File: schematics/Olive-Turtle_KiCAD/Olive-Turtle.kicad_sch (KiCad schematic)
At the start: 14 parts, among them IC1 ENS160-BGLT, U1 ESP32-DEVKITC-32U

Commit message: Designed VeeCAD schematic
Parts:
- renumbered L1-T2 to L1-T1, L1-T1 to L2-T1
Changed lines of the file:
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@@
   (symbol (lib_id "IRF520:IRF520") (at 74.93 78.74 0) (mirror y) (unit 1)
     (in_bom yes) (on_board yes) (dnp no)
-    (property "Reference" "L1-T2" (at 67.31 79.158 0)
+    (property "Reference" "L1-T1" (at 67.31 79.158 0)
       (effects (font (size 1.27 1.27)) (justify left))
     )
@@
       (project "Olive-Turtle"
         (path "/51055cea-6c3b-4d6e-9886-de884be04eed"
-          (reference "L1-T2") (unit 1)
+          (reference "L1-T1") (unit 1)
         )
       )
@@
   (symbol (lib_id "IRF520:IRF520") (at 40.64 96.52 0) (mirror y) (unit 1)
     (in_bom yes) (on_board yes) (dnp no)
-    (property "Reference" "L1-T1" (at 33.02 96.938 0)
+    (property "Reference" "L2-T1" (at 33.02 96.938 0)
       (effects (font (size 1.27 1.27)) (justify left))
     )
@@
       (project "Olive-Turtle"
         (path "/51055cea-6c3b-4d6e-9886-de884be04eed"
-          (reference "L1-T1") (unit 1)
-        )
-      )
+          (reference "L2-T1") (unit 1)
+        )
+      )

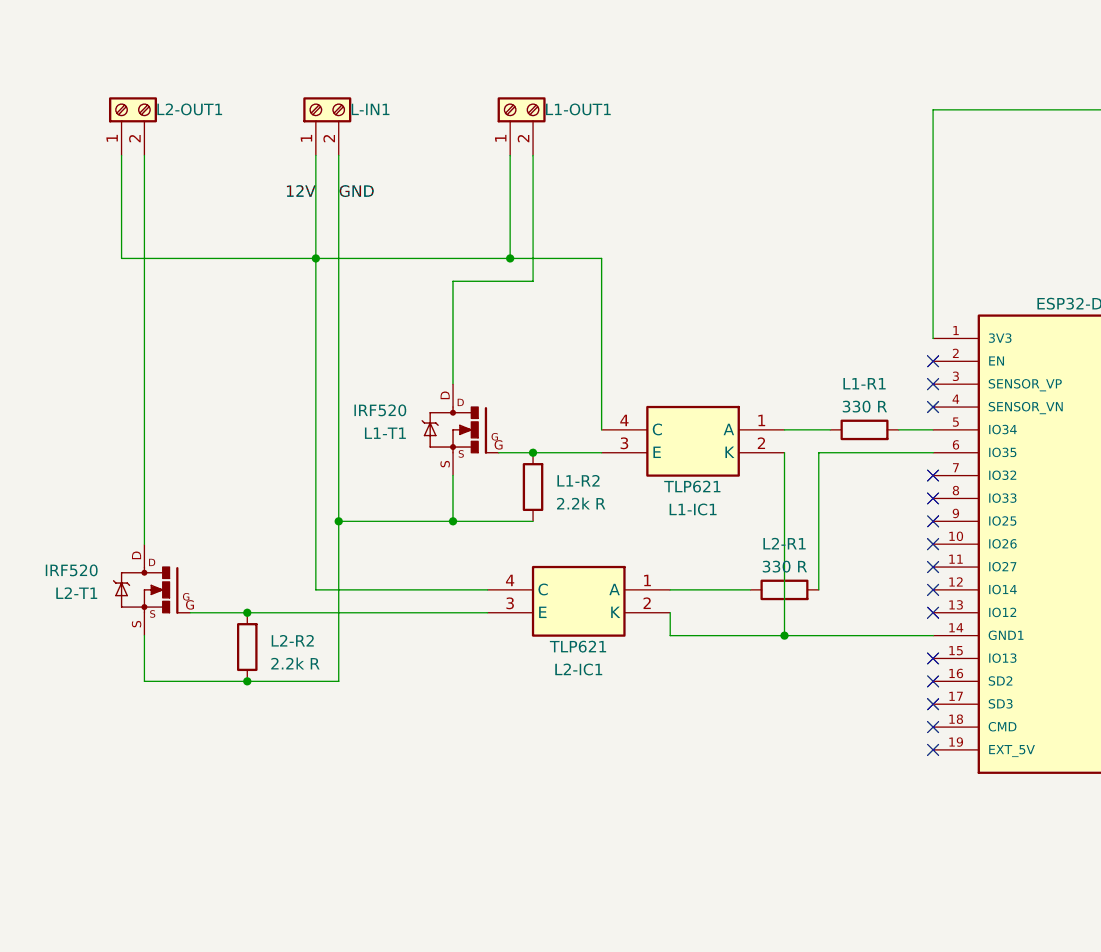
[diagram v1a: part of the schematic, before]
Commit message: [develop] Schematic for LC
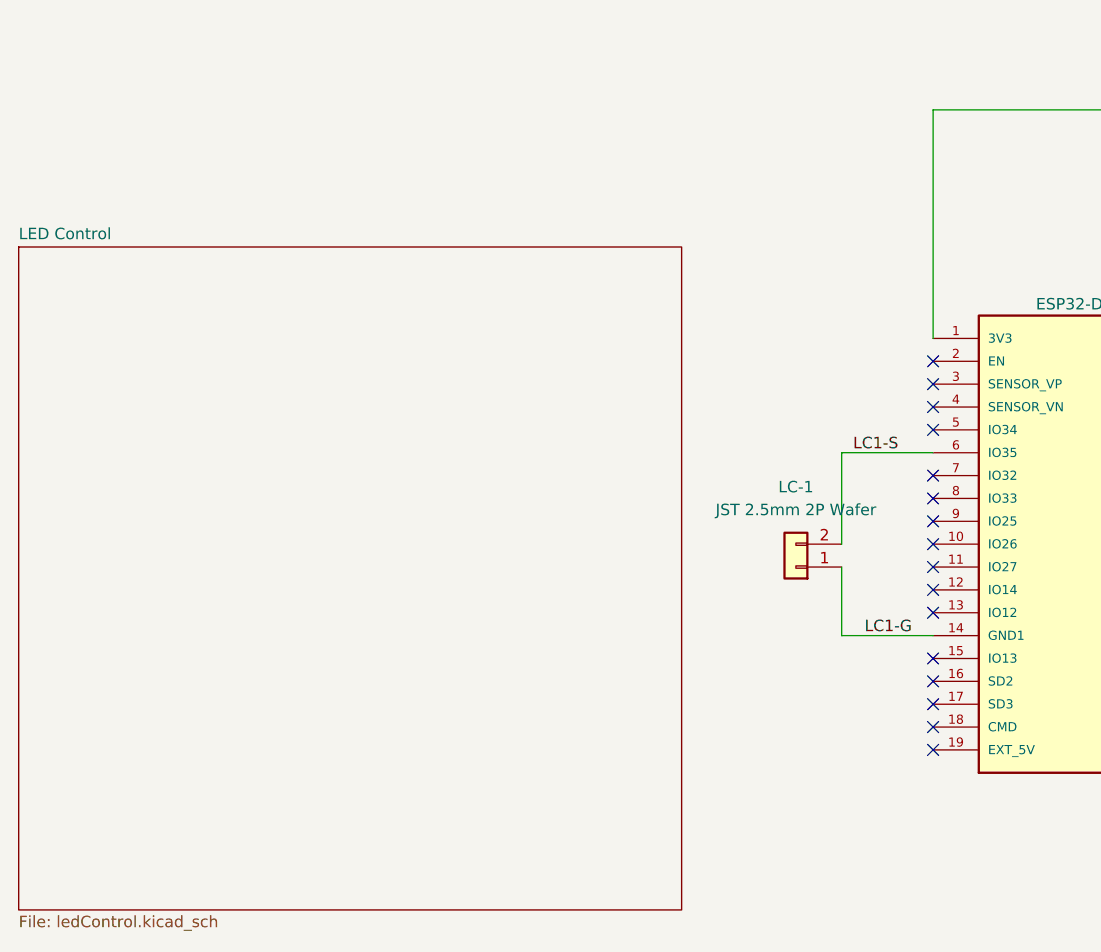
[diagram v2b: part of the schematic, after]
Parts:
- removed L-IN1, L1-OUT1, L2-OUT1: Screw_Terminal_01x02, TerminalBlock:TerminalBlock_bornier-2_P5.08mm, symbol Connector:Screw_Terminal_01x02
- removed L1-IC1, L2-IC1: TLP621, DIP762W60P254L460H450Q4N, symbol TLP621:TLP621
- removed L1-R1, L2-R1: 330 R, symbol Device:R
- removed L1-R2, L2-R2: 2.2k R, symbol Device:R
- removed L1-T1, L2-T1: IRF520, TO220BV, symbol IRF520:IRF520
- added LC-1: JST 2.5mm 2P Wafer, Connector_JST:JST_EH_B2B-EH-A_1x02_P2.50mm_Vertical, symbol Connector_Generic:Conn_01x02
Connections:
- net LC1-G: now reaches U1.14 (GND1)
- net LC1-G: now also LC-1.1 (Pin_1)
- net LC1-S: now reaches U1.6 (IO35)
- net LC1-S: now also LC-1.2 (Pin_2)
- no-connect marks 38 -> 39
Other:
- added sheet LED Control (ledControl.kicad_sch)

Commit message: [develop] Update Kicad schematic
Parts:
- added L-IN1, L1-OUT1: Screw_Terminal_01x02, TerminalBlock:TerminalBlock_bornier-2_P5.08mm, symbol Connector:Screw_Terminal_01x02
- added L1-IC1: TLP621, DIP762W60P254L460H450Q4N, symbol TLP621:TLP621
- added L1-R1: 2.2k R, Resistor_THT:R_Axial_DIN0204_L3.6mm_D1.6mm_P7.62mm_Horizontal, symbol Device:R
- added L1-R2: 330 R, Resistor_THT:R_Axial_DIN0204_L3.6mm_D1.6mm_P7.62mm_Horizontal, symbol Device:R
- added L1-T1: IRF520, TO220BV, symbol IRF520:IRF520
- added LC-2: JST 2.5mm 2P Wafer, Connector_JST:JST_EH_B2B-EH-A_1x02_P2.50mm_Vertical, symbol Connector_Generic:Conn_01x02
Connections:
- new net: L1-OUT1.2 (Pin_2), L1-T1.D
- new net: L1-IC1.3 (E), L1-R1.2, L1-T1.G
- new net: L1-IC1.1 (A), L1-R2.1
- new net 12V: L-IN1.1 (Pin_1), L1-IC1.4 (C), L1-OUT1.1 (Pin_1)
- new net GND: L-IN1.2 (Pin_2), L1-R1.1, L1-T1.S
- new net LC-G: L1-IC1.2 (K), LC-2.1 (Pin_1)
- new net LC-S: L1-R2.2, LC-2.2 (Pin_2)
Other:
- removed sheet LED Control

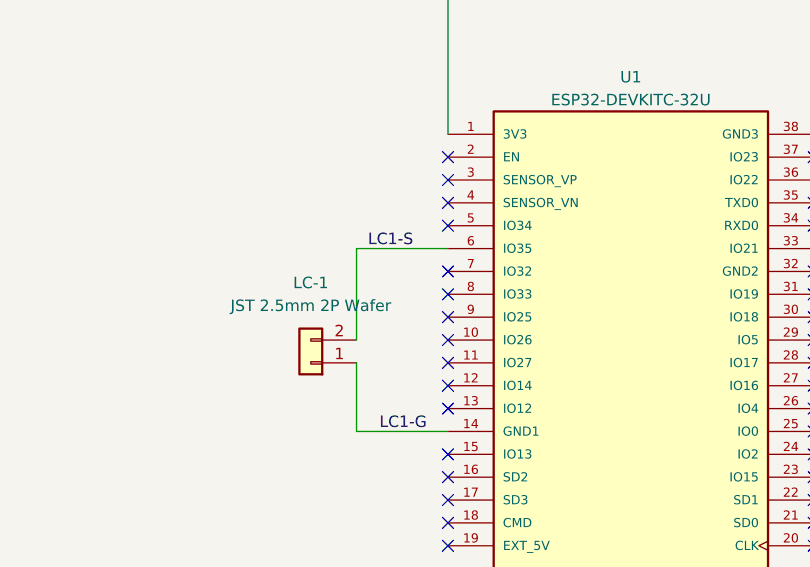
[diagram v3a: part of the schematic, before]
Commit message: [develop] Move LED1 to pin 32 since 35 is input only
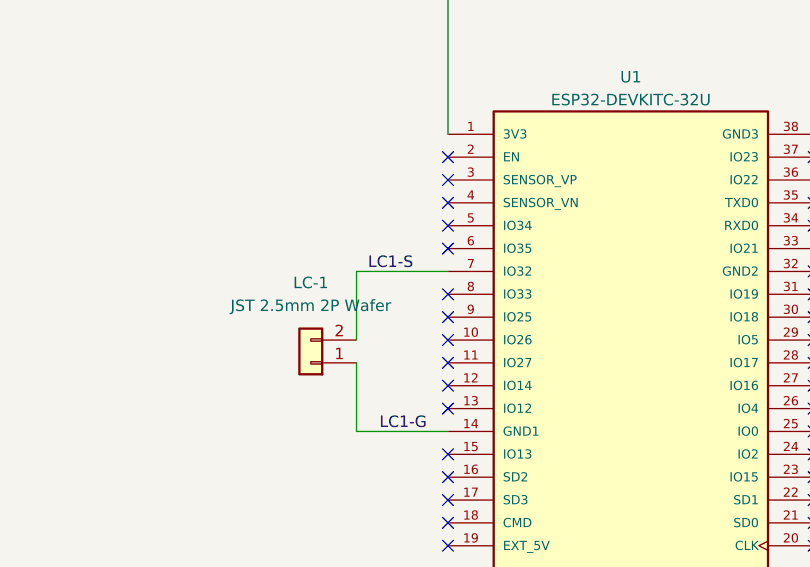
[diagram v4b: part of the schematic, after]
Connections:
- net LC1-S: now also U1.7 (IO32); no longer U1.6 (IO35)
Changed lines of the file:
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@@
   (no_connect (at 125.73 114.3))
   (no_connect (at 125.73 109.22))
-  (no_connect (at 125.73 83.82))
   (no_connect (at 125.73 106.68))
   (no_connect (at 166.37 101.6))
@@
   (no_connect (at 232.41 97.79))
   (no_connect (at 166.37 96.52))
+  (no_connect (at 125.73 81.28))
   (no_connect (at 166.37 86.36))
   (no_connect (at 166.37 71.12))
@@
     (stroke (width 0) (type default))
   )
-  (wire (pts (xy 115.57 91.44) (xy 115.57 81.28))
+  (wire (pts (xy 115.57 91.44) (xy 115.57 83.82))
     (stroke (width 0) (type default))
   )
@@
     (stroke (width 0) (type default))
   )
-  (wire (pts (xy 115.57 81.28) (xy 125.73 81.28))
+  (wire (pts (xy 115.57 83.82) (xy 125.73 83.82))
     (stroke (width 0) (type default))
   )
@@
     (effects (font (size 1.27 1.27)) (justify left bottom))
   )
-  (label "LC1-S" (at 116.84 81.28 0) (fields_autoplaced)
+  (label "LC1-S" (at 116.84 83.82 0) (fields_autoplaced)
     (effects (font (size 1.27 1.27)) (justify left bottom))
   )

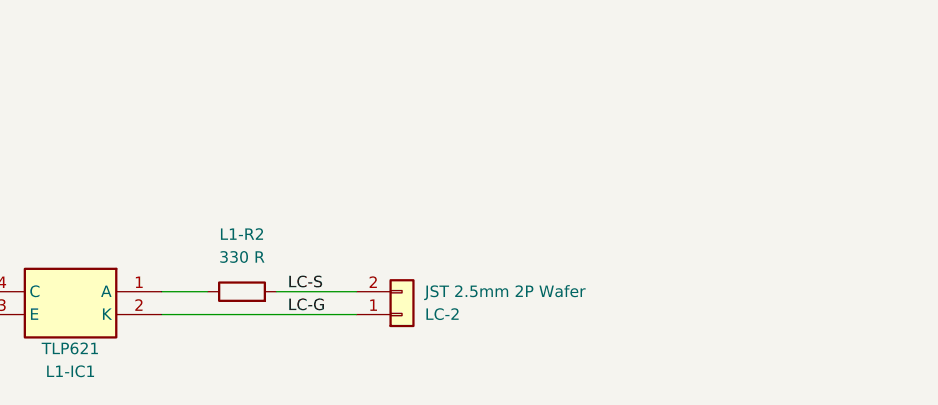
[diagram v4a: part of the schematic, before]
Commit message: [develop] Add led to control circuit
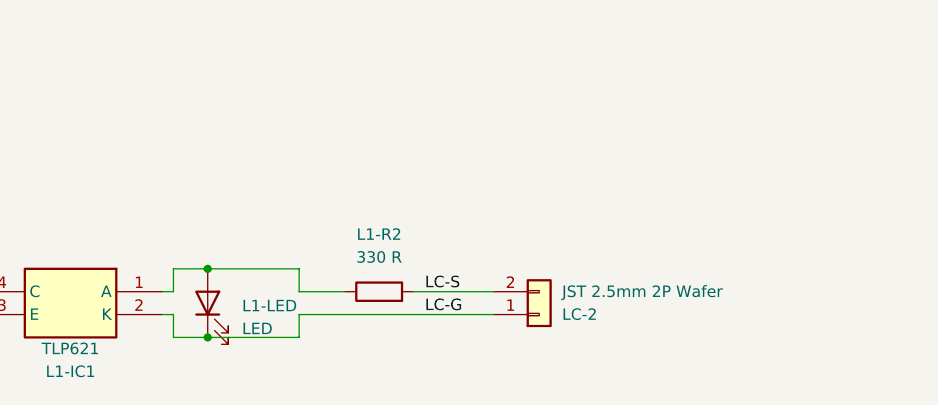
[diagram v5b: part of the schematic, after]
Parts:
- added L1-LED: LED, symbol Device:LED
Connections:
- net LC-G: now also L1-LED.1 (K)
- net at L1-IC1.1 (A), L1-R2.1: now also L1-LED.2 (A)
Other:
- title: Olive Turtle Project -> Olive Turtle Project - Led Control
- moved on the sheet: L1-R2, LC-2
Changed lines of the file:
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@@
   (paper "A4")
   (title_block
-    (title "Olive Turtle Project")
-    (date "2023-05-14")
-    (rev "1.0")
+    (title "Olive Turtle Project - Led Control")
+    (date "2023-09-21")
+    (rev "2.0")
   )
   (junction (at 191.77 43.18) (diameter 0) (color 0 0 0 0)
   )
+  (junction (at 99.06 148.59) (diameter 0) (color 0 0 0 0)
+  )
   (junction (at 66.04 153.67) (diameter 0) (color 0 0 0 0)
+  )
+  (junction (at 99.06 156.21) (diameter 0) (color 0 0 0 0)
   )
   (junction (at 220.98 68.58) (diameter 0) (color 0 0 0 0)
@@
     (stroke (width 0) (type default))
   )
-  (wire (pts (xy 93.98 151.13) (xy 99.06 151.13))
-    (stroke (width 0) (type default))
-  )
   (wire (pts (xy 204.47 73.66) (xy 204.47 50.8))
     (stroke (width 0) (type default))
@@
     (stroke (width 0) (type default))
   )
+  (wire (pts (xy 114.3 151.13) (xy 109.22 151.13))
+    (stroke (width 0) (type default))
+  )
   (wire (pts (xy 73.66 132.08) (xy 63.5 132.08))
     (stroke (width 0) (type default))
@@
     (stroke (width 0) (type default))
   )
+  (wire (pts (xy 95.25 153.67) (xy 95.25 156.21))
+    (stroke (width 0) (type default))
+  )
   (wire (pts (xy 166.37 81.28) (xy 194.31 81.28))
     (stroke (width 0) (type default))
@@
     (stroke (width 0) (type default))
   )
-  (wire (pts (xy 106.68 151.13) (xy 115.57 151.13))
+  (wire (pts (xy 121.92 151.13) (xy 130.81 151.13))
     (stroke (width 0) (type default))
   )
@@
     (stroke (width 0) (type default))
   )
+  (wire (pts (xy 93.98 151.13) (xy 95.25 151.13))
+    (stroke (width 0) (type default))
+  )
   (wire (pts (xy 194.31 92.71) (xy 190.5 92.71))
     (stroke (width 0) (type default))
   )
+  (wire (pts (xy 95.25 148.59) (xy 99.06 148.59))
+    (stroke (width 0) (type default))
+  )
+  (wire (pts (xy 130.81 153.67) (xy 109.22 153.67))
+    (stroke (width 0) (type default))
+  )
+  (wire (pts (xy 109.22 156.21) (xy 99.06 156.21))
+    (stroke (width 0) (type default))
+  )
   (wire (pts (xy 191.77 57.15) (xy 191.77 43.18))
     (stroke (width 0) (type default))
@@
     (stroke (width 0) (type default))
   )
+  (wire (pts (xy 95.25 156.21) (xy 99.06 156.21))
+    (stroke (width 0) (type default))
+  )
   (wire (pts (xy 115.57 83.82) (xy 125.73 83.82))
     (stroke (width 0) (type default))
@@
     (stroke (width 0) (type default))
   )
+  (wire (pts (xy 109.22 148.59) (xy 99.06 148.59))
+    (stroke (width 0) (type default))
+  )
+  (wire (pts (xy 95.25 151.13) (xy 95.25 148.59))
+    (stroke (width 0) (type default))
+  )
   (wire (pts (xy 125.73 68.58) (xy 125.73 43.18))
     (stroke (width 0) (type default))
   )
+  (wire (pts (xy 109.22 151.13) (xy 109.22 148.59))
+    (stroke (width 0) (type default))
+  )
   (wire (pts (xy 190.5 92.71) (xy 190.5 73.66))
     (stroke (width 0) (type default))
   )
+  (wire (pts (xy 93.98 153.67) (xy 95.25 153.67))
+    (stroke (width 0) (type default))
+  )
+  (wire (pts (xy 109.22 153.67) (xy 109.22 156.21))
+    (stroke (width 0) (type default))
+  )
   (wire (pts (xy 194.31 100.33) (xy 191.77 100.33))
     (stroke (width 0) (type default))
   )
   (wire (pts (xy 66.04 134.62) (xy 57.15 134.62))
-    (stroke (width 0) (type default))
-  )
-  (wire (pts (xy 93.98 153.67) (xy 115.57 153.67))
     (stroke (width 0) (type default))
   )
@@
     (effects (font (size 1.27 1.27)) (justify right bottom))
   )
-  (label "LC-S" (at 107.95 151.13 0) (fields_autoplaced)
+  (label "LC-S" (at 123.19 151.13 0) (fields_autoplaced)
     (effects (font (size 1.27 1.27)) (justify left bottom))
   )
@@
     (effects (font (size 1.27 1.27)) (justify left bottom))
   )
-  (label "LC-G" (at 107.95 153.67 0) (fields_autoplaced)
+  (label "LC-G" (at 123.19 153.67 0) (fields_autoplaced)
     (effects (font (size 1.27 1.27)) (justify left bottom))
   )
@@
     )
   )
-  (symbol (lib_id "Device:R") (at 102.87 151.13 90) (unit 1)
+  (symbol (lib_id "Device:R") (at 118.11 151.13 90) (unit 1)
     (in_bom yes) (on_board yes) (dnp no) (fields_autoplaced)
-    (property "Reference" "L1-R2" (at 102.87 144.78 90)
-      (effects (font (size 1.27 1.27)))
-    )
-    (property "Value" "330 R" (at 102.87 147.32 90)
-      (effects (font (size 1.27 1.27)))
-    )
-    (property "Footprint" "Resistor_THT:R_Axial_DIN0204_L3.6mm_D1.6mm_P7.62mm_Horizontal" (at 102.87 152.908 90)
-      (effects (font (size 1.27 1.27)) hide)
-    )
-    (property "Datasheet" "~" (at 102.87 151.13 0)
+    (property "Reference" "L1-R2" (at 118.11 144.78 90)
+      (effects (font (size 1.27 1.27)))
+    )
+    (property "Value" "330 R" (at 118.11 147.32 90)
+      (effects (font (size 1.27 1.27)))
+    )
+    (property "Footprint" "Resistor_THT:R_Axial_DIN0204_L3.6mm_D1.6mm_P7.62mm_Horizontal" (at 118.11 152.908 90)
+      (effects (font (size 1.27 1.27)) hide)
+    )
+    (property "Datasheet" "~" (at 118.11 151.13 0)
       (effects (font (size 1.27 1.27)) hide)
     )
@@
     )
   )
-  (symbol (lib_id "Connector_Generic:Conn_01x02") (at 120.65 153.67 0) (mirror x) (unit 1)
+  (symbol (lib_id "Device:LED") (at 99.06 152.4 90) (unit 1)
     (in_bom yes) (on_board yes) (dnp no)
-    (property "Reference" "LC-2" (at 123.19 153.67 0)
+    (property "Reference" "L1-LED" (at 102.87 152.7175 90)
+      (effects (font (size 1.27 1.27)) (justify right))
+    )
+    (property "Value" "LED" (at 102.87 155.2575 90)
+      (effects (font (size 1.27 1.27)) (justify right))
+    )
+    (property "Footprint" "" (at 99.06 152.4 0)
+      (effects (font (size 1.27 1.27)) hide)
+    )
+    (property "Datasheet" "~" (at 99.06 152.4 0)
+      (effects (font (size 1.27 1.27)) hide)
+    )
+    (pin "1")
+    (pin "2")
+    (instances
+      (project "Olive-Turtle"
+        (path "/51055cea-6c3b-4d6e-9886-de884be04eed"
+          (reference "L1-LED") (unit 1)
+        )
+      )
+    )
+  )
+  (symbol (lib_id "Connector_Generic:Conn_01x02") (at 135.89 153.67 0) (mirror x) (unit 1)
+    (in_bom yes) (on_board yes) (dnp no)
+    (property "Reference" "LC-2" (at 138.43 153.67 0)
       (effects (font (size 1.27 1.27)) (justify left))
     )
-    (property "Value" "JST 2.5mm 2P Wafer" (at 123.19 151.13 0)
+    (property "Value" "JST 2.5mm 2P Wafer" (at 138.43 151.13 0)
       (effects (font (size 1.27 1.27)) (justify left))
     )
-    (property "Footprint" "Connector_JST:JST_EH_B2B-EH-A_1x02_P2.50mm_Vertical" (at 120.65 153.67 0)
-      (effects (font (size 1.27 1.27)) hide)
-    )
-    (property "Datasheet" "~" (at 120.65 153.67 0)
-      (effects (font (size 1.27 1.27)) hide)
-    )
+    (property "Footprint" "Connector_JST:JST_EH_B2B-EH-A_1x02_P2.50mm_Vertical" (at 135.89 153.67 0)
+      (effects (font (size 1.27 1.27)) hide)
+    )
+    (property "Datasheet" "~" (at 135.89 153.67 0)
+      (effects (font (size 1.27 1.27)) hide)
+    )
